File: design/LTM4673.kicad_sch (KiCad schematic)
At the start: 96 parts, among them U35 LTM4673IY#PBF

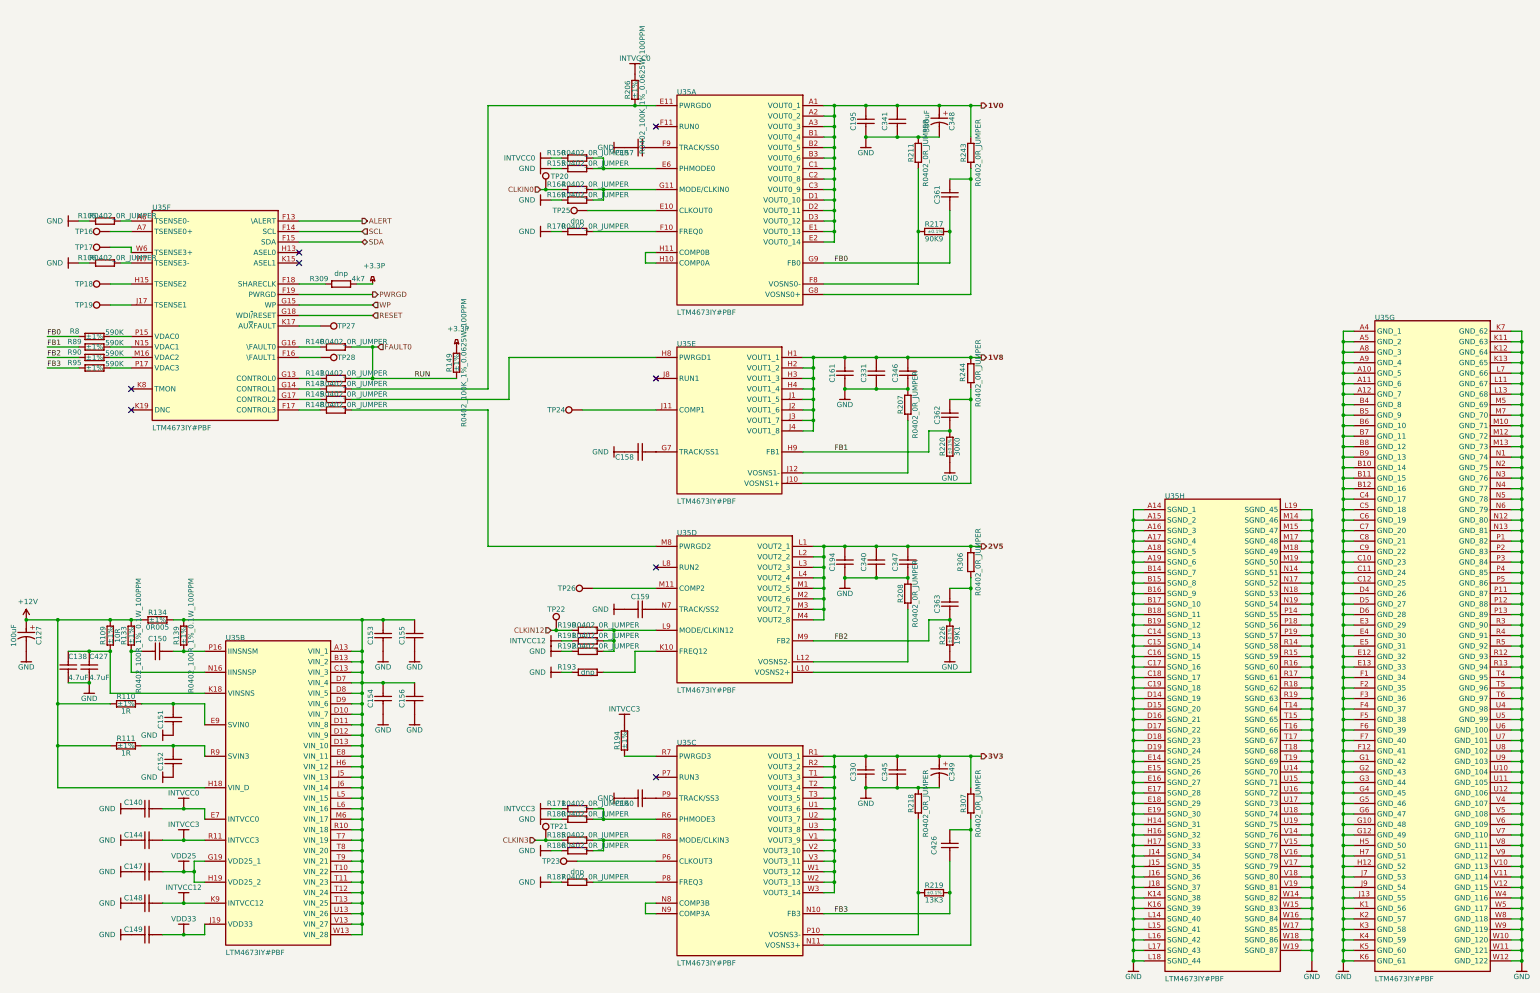
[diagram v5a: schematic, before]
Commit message: TAG connector added, descriptions for connectors added
TAG connector added, descriptions for connectors added
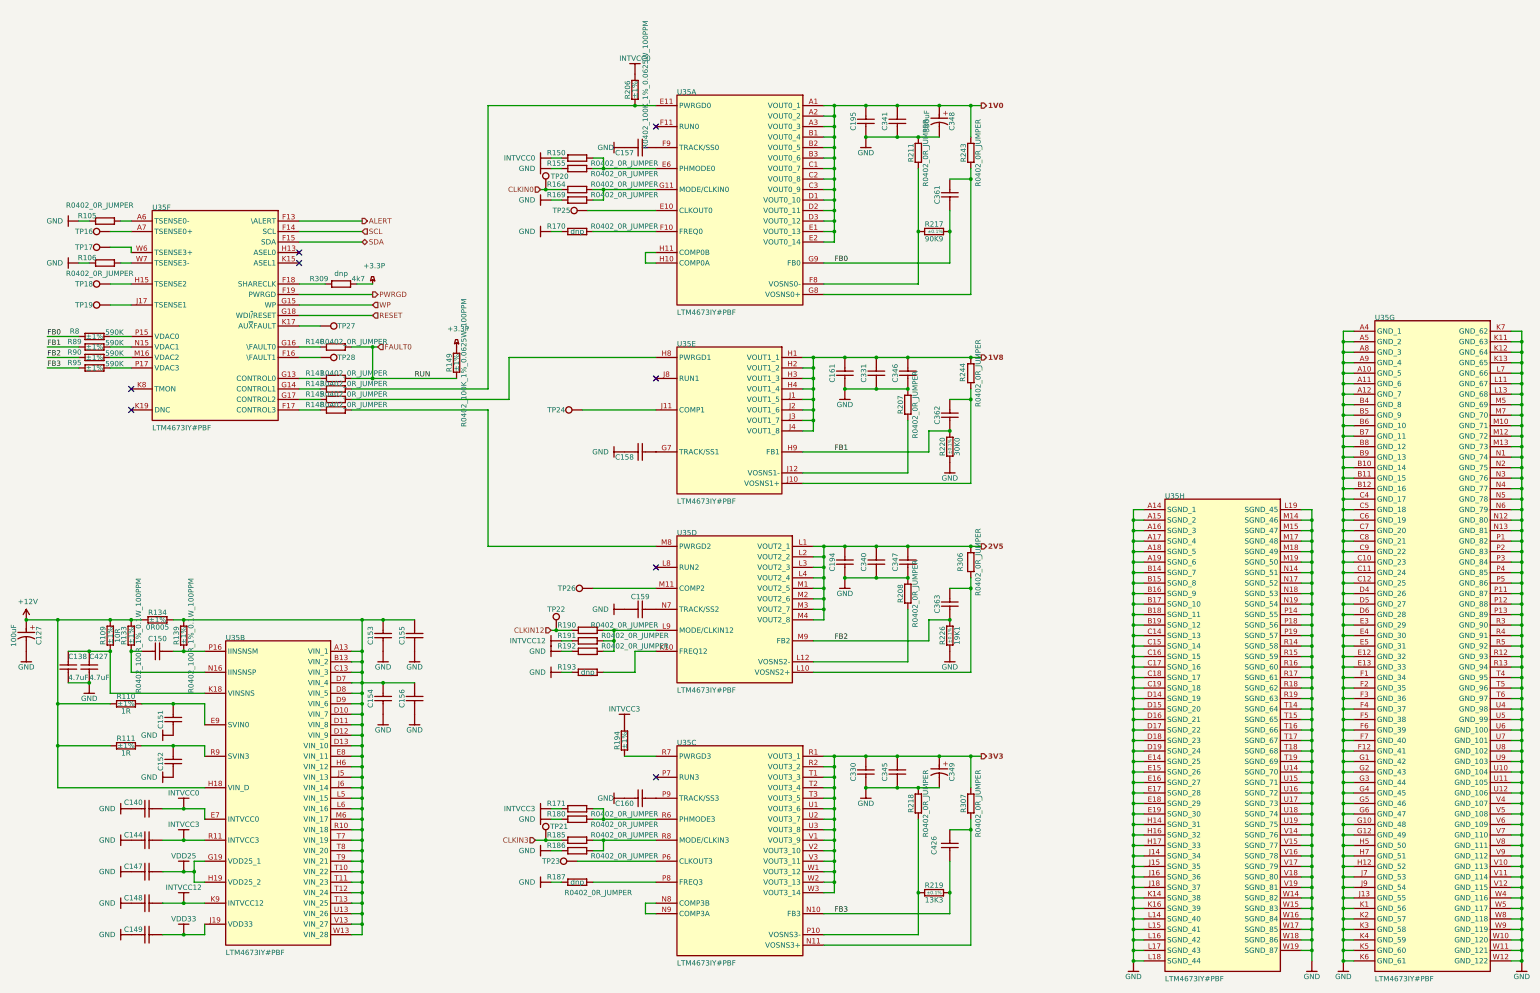
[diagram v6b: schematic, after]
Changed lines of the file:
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@@
     (in_bom yes) (on_board yes)
     (property "Reference" "R150" (id 0) (at 157.48 49.53 0))
-    (property "Value" "R0402_0R_JUMPER" (id 1) (at 166.878 49.53 0))
+    (property "Value" "R0402_0R_JUMPER" (id 1) (at 173.99 52.07 0))
     (property "Footprint" "RESC1005X40N" (id 2) (at 158.75 50.8 0)
       (effects (font (size 1.27 1.27)) hide)
@@
     (in_bom yes) (on_board yes)
     (property "Reference" "R186" (id 0) (at 157.48 217.17 0))
-    (property "Value" "R0402_0R_JUMPER" (id 1) (at 166.878 217.17 0))
+    (property "Value" "R0402_0R_JUMPER" (id 1) (at 173.99 219.71 0))
     (property "Footprint" "RESC1005X40N" (id 2) (at 158.75 218.44 0)
       (effects (font (size 1.27 1.27)) hide)
@@
     (in_bom yes) (on_board yes)
     (property "Reference" "R164" (id 0) (at 157.48 57.15 0))
-    (property "Value" "R0402_0R_JUMPER" (id 1) (at 166.878 57.15 0))
+    (property "Value" "R0402_0R_JUMPER" (id 1) (at 173.99 57.15 0))
     (property "Footprint" "RESC1005X40N" (id 2) (at 158.75 58.42 0)
       (effects (font (size 1.27 1.27)) hide)
@@
     (in_bom yes) (on_board yes)
     (property "Reference" "R190" (id 0) (at 160.02 163.83 0))
-    (property "Value" "R0402_0R_JUMPER" (id 1) (at 169.418 163.83 0))
+    (property "Value" "R0402_0R_JUMPER" (id 1) (at 173.99 163.83 0))
     (property "Footprint" "RESC1005X40N" (id 2) (at 161.29 165.1 0)
       (effects (font (size 1.27 1.27)) hide)
@@
     (in_bom yes) (on_board yes)
     (property "Reference" "R171" (id 0) (at 157.48 207.01 0))
-    (property "Value" "R0402_0R_JUMPER" (id 1) (at 166.878 207.01 0))
+    (property "Value" "R0402_0R_JUMPER" (id 1) (at 173.99 209.55 0))
     (property "Footprint" "RESC1005X40N" (id 2) (at 158.75 208.28 0)
       (effects (font (size 1.27 1.27)) hide)
@@
     (in_bom yes) (on_board yes)
     (property "Reference" "R170" (id 0) (at 157.48 67.31 0))
-    (property "Value" "R0402_0R_JUMPER" (id 1) (at 166.878 67.31 0))
+    (property "Value" "R0402_0R_JUMPER" (id 1) (at 173.99 67.31 0))
     (property "Footprint" "RESC1005X40N" (id 2) (at 158.75 68.58 0)
       (effects (font (size 1.27 1.27)) hide)
@@
       (effects (font (size 1.27 1.27)) (justify left bottom) hide)
     )
-    (property "config" "dnp" (id 27) (at 162.56 66.04 0))
+    (property "config" "dnp" (id 27) (at 162.56 68.58 0))
     (property "Manufacturer Part Number" "R0402_0R_JUMPER" (id 28) (at 158.75 68.58 0)
       (effects (font (size 1.27 1.27)) hide)
@@
     (in_bom yes) (on_board yes)
     (property "Reference" "R180" (id 0) (at 157.48 209.55 0))
-    (property "Value" "R0402_0R_JUMPER" (id 1) (at 166.878 209.55 0))
+    (property "Value" "R0402_0R_JUMPER" (id 1) (at 173.99 212.09 0))
     (property "Footprint" "RESC1005X40N" (id 2) (at 158.75 210.82 0)
       (effects (font (size 1.27 1.27)) hide)
@@
     (in_bom yes) (on_board yes)
     (property "Reference" "R192" (id 0) (at 160.02 168.91 0))
-    (property "Value" "R0402_0R_JUMPER" (id 1) (at 169.418 168.91 0))
+    (property "Value" "R0402_0R_JUMPER" (id 1) (at 176.53 168.91 0))
     (property "Footprint" "RESC1005X40N" (id 2) (at 161.29 170.18 0)
       (effects (font (size 1.27 1.27)) hide)
@@
     (in_bom yes) (on_board yes)
     (property "Reference" "R206" (id 0) (at 174.752 34.29 90))
-    (property "Value" "R0402_100K_1%_0.0625W_100PPM" (id 1) (at 178.308 34.29 90))
+    (property "Value" "R0402_100K_1%_0.0625W_100PPM" (id 1) (at 179.07 33.02 90))
     (property "Footprint" "RESC1005X40N" (id 2) (at 176.53 38.1 0)
       (effects (font (size 1.27 1.27)) hide)
@@
     (in_bom yes) (on_board yes)
     (property "Reference" "R191" (id 0) (at 160.02 166.37 0))
-    (property "Value" "R0402_0R_JUMPER" (id 1) (at 169.418 166.37 0))
+    (property "Value" "R0402_0R_JUMPER" (id 1) (at 176.53 166.37 0))
     (property "Footprint" "RESC1005X40N" (id 2) (at 161.29 167.64 0)
       (effects (font (size 1.27 1.27)) hide)
@@
     (in_bom yes) (on_board yes)
     (property "Reference" "R155" (id 0) (at 157.48 52.07 0))
-    (property "Value" "R0402_0R_JUMPER" (id 1) (at 166.878 52.07 0))
+    (property "Value" "R0402_0R_JUMPER" (id 1) (at 173.99 54.61 0))
     (property "Footprint" "RESC1005X40N" (id 2) (at 158.75 53.34 0)
       (effects (font (size 1.27 1.27)) hide)
@@
     (in_bom yes) (on_board yes)
     (property "Reference" "R106" (id 0) (at 43.942 74.93 0))
-    (property "Value" "R0402_0R_JUMPER" (id 1) (at 52.578 74.93 0))
+    (property "Value" "R0402_0R_JUMPER" (id 1) (at 46.99 78.74 0))
     (property "Footprint" "RESC1005X40N" (id 2) (at 44.45 76.2 0)
       (effects (font (size 1.27 1.27)) hide)
@@
     (in_bom yes) (on_board yes)
     (property "Reference" "R185" (id 0) (at 157.48 214.63 0))
-    (property "Value" "R0402_0R_JUMPER" (id 1) (at 166.878 214.63 0))
+    (property "Value" "R0402_0R_JUMPER" (id 1) (at 173.99 214.63 0))
     (property "Footprint" "RESC1005X40N" (id 2) (at 158.75 215.9 0)
       (effects (font (size 1.27 1.27)) hide)
@@
     (in_bom yes) (on_board yes)
     (property "Reference" "R105" (id 0) (at 43.942 64.77 0))
-    (property "Value" "R0402_0R_JUMPER" (id 1) (at 52.578 64.77 0))
+    (property "Value" "R0402_0R_JUMPER" (id 1) (at 46.99 62.23 0))
     (property "Footprint" "RESC1005X40N" (id 2) (at 44.45 66.04 0)
       (effects (font (size 1.27 1.27)) hide)
@@
     (in_bom yes) (on_board yes)
     (property "Reference" "R169" (id 0) (at 157.48 59.69 0))
-    (property "Value" "R0402_0R_JUMPER" (id 1) (at 166.878 59.69 0))
+    (property "Value" "R0402_0R_JUMPER" (id 1) (at 173.99 59.69 0))
     (property "Footprint" "RESC1005X40N" (id 2) (at 158.75 60.96 0)
       (effects (font (size 1.27 1.27)) hide)
@@
     (in_bom yes) (on_board yes)
     (property "Reference" "R187" (id 0) (at 157.48 224.79 0))
-    (property "Value" "R0402_0R_JUMPER" (id 1) (at 166.878 224.79 0))
+    (property "Value" "R0402_0R_JUMPER" (id 1) (at 167.64 228.6 0))
     (property "Footprint" "RESC1005X40N" (id 2) (at 158.75 226.06 0)
       (effects (font (size 1.27 1.27)) hide)
@@
       (effects (font (size 1.27 1.27)) hide)
     )
-    (property "config" "dnp" (id 28) (at 162.56 223.52 0))
+    (property "config" "dnp" (id 28) (at 162.56 226.06 0))
     (pin "1")
     (pin "2")
